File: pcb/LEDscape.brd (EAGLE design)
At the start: 133.3 x 88.9 mm, 30 parts, among them IC1 MAX3041CUE, IC2 MAX3041CUE, IC3 MAX3041CUE, IC4 MAX3041CUE, IC5 MAX3041CUE, IC6 MAX3041CUE, IC7 MAX3041CUE, IC8 MAX3041CUE, X1 44520-0003

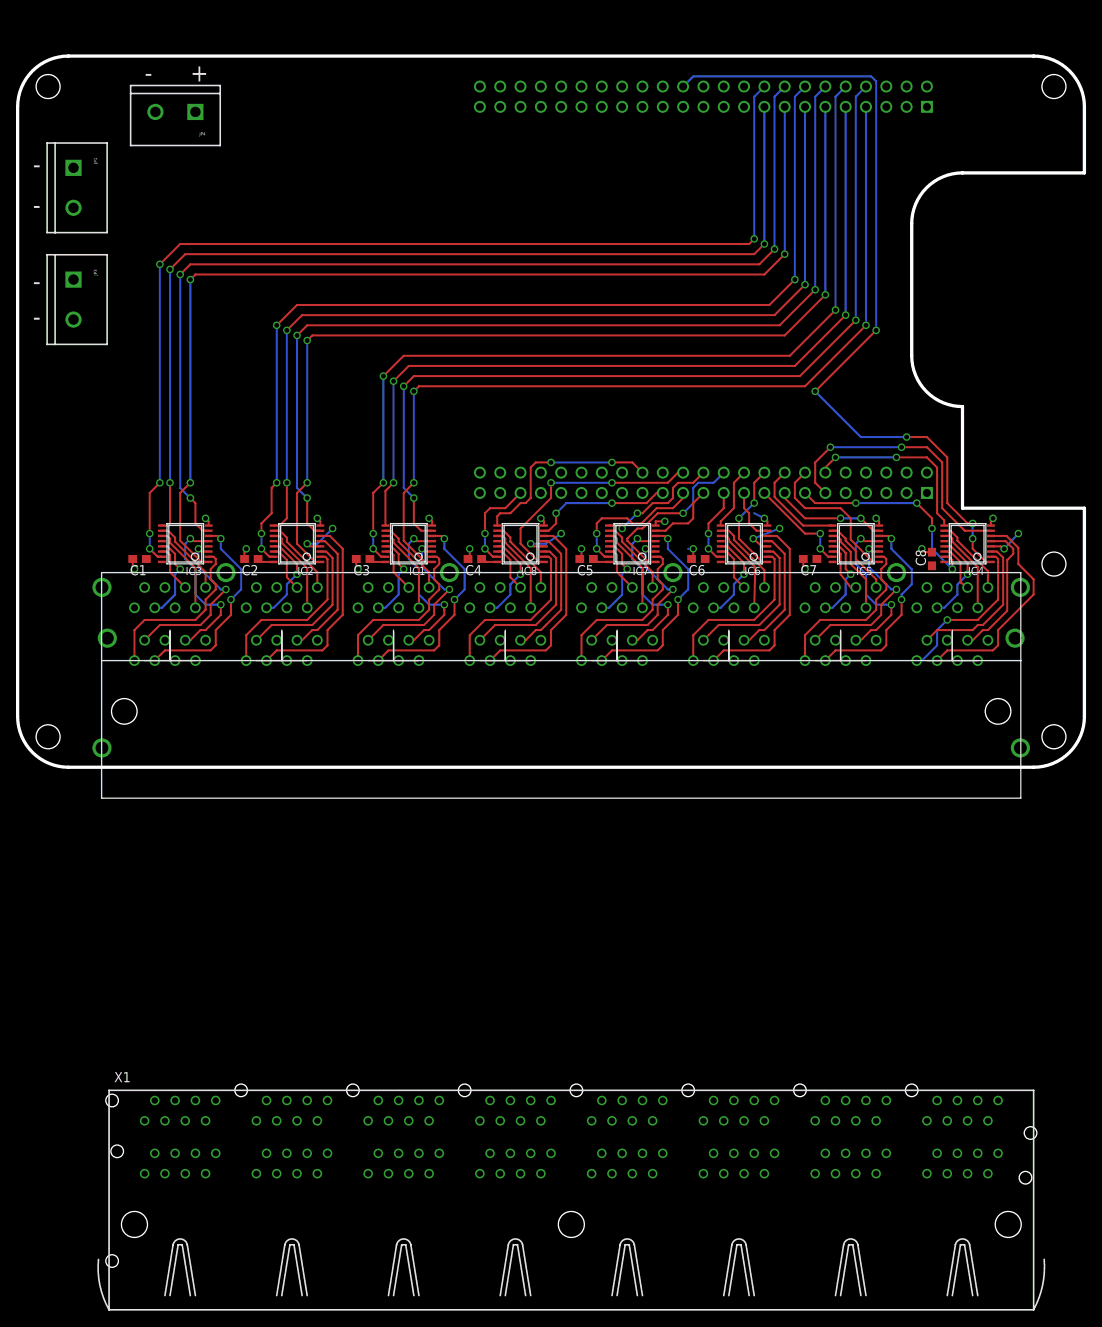
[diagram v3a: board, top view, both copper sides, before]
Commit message: Add some expansion IO (conflicts with HDMI, beware), and fix 8x2 header
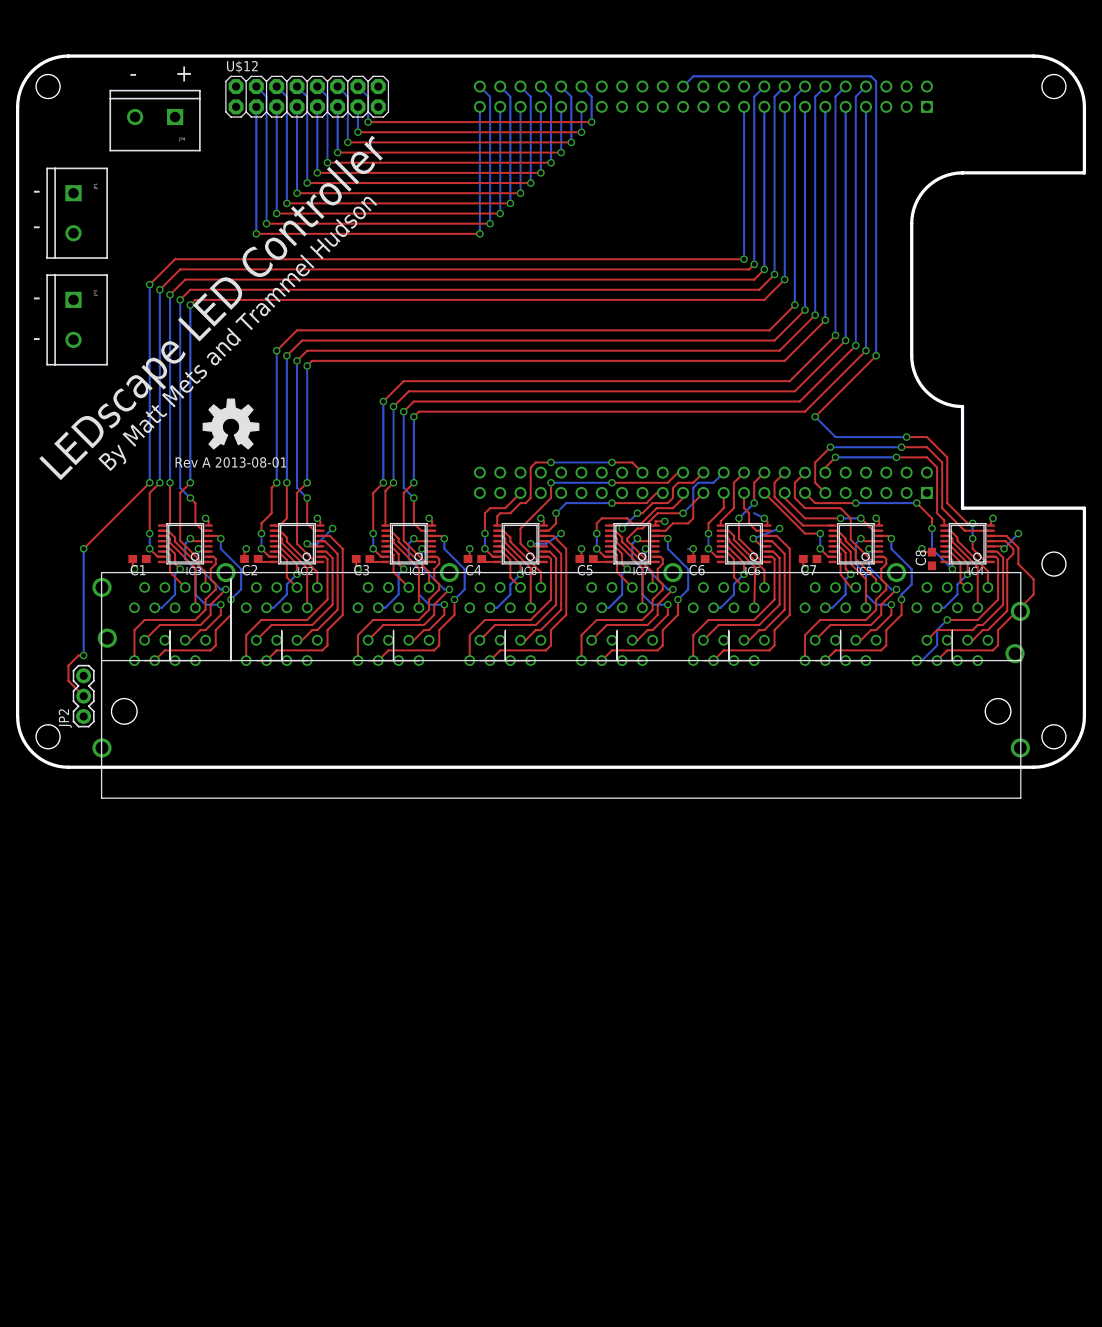
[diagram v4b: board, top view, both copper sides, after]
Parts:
- removed X1: 44520-0003, con-molex:44520-0003
- added JP2: (no value), SparkFun-Connectors:1X03
- added U$11: (no value), blinkiverse:OSHW-LOGO-L
- added U$12: M08X2, SparkFun-Connectors:2X8
- moved JP1 3.18 mm to (6.99, 71.8)
- moved JP4 2.62 mm to (19.7, 81.3)
- moved JP3 2.54 mm to (6.99, 58.4)
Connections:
- new net E0: U$1.45, U$12.3
- new net E1: U$1.46, U$12.4
- new net E10: U$1.35, U$12.13
- new net E11: U$1.36, U$12.14
- new net E2: U$1.43, U$12.5
- new net E3: U$1.44, U$12.6
- new net E4: U$1.41, U$12.7
- new net E5: U$1.42, U$12.8
- new net E6: U$1.39, U$12.9
- new net E7: U$1.40, U$12.10
- new net E8: U$1.37, U$12.11
- new net E9: U$1.38, U$12.12
- new net EXTRA0: JP2.2, U$1.19
- net +5V: now also JP2.1, U$12.1, U$12.2
- net GND: now also JP2.3, U$12.15, U$12.16
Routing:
- net EXTRA0: track 0.00 -> 151.5 mm, vias 0 -> 5
- net E1: track 0.00 -> 63.3 mm, vias 0 -> 2
- net E0: track 0.00 -> 59.7 mm, vias 0 -> 2
- net E3: track 0.00 -> 58.2 mm, vias 0 -> 2
- net E2: track 0.00 -> 54.6 mm, vias 0 -> 2
- net E5: track 0.00 -> 53.1 mm, vias 0 -> 2
- net E4: track 0.00 -> 49.5 mm, vias 0 -> 2
- net E7: track 0.00 -> 48.0 mm, vias 0 -> 2
- net E6: track 0.00 -> 44.4 mm, vias 0 -> 2
- net E9: track 0.00 -> 43.0 mm, vias 0 -> 2
- net E8: track 0.00 -> 39.4 mm, vias 0 -> 2
- net E11: track 0.00 -> 37.9 mm, vias 0 -> 2
- net E10: track 0.00 -> 34.3 mm, vias 0 -> 2
- net S12: track 102.8 -> 104.7 mm
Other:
- board text added: "By Matt Mets and Trammel Hudson"
- board text added: "LEDscape LED Controller"
- board text added: "Rev A 2013-08-01"

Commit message: Small cleanups; take part identifiers off silk, change outline of ethernet to tDocu
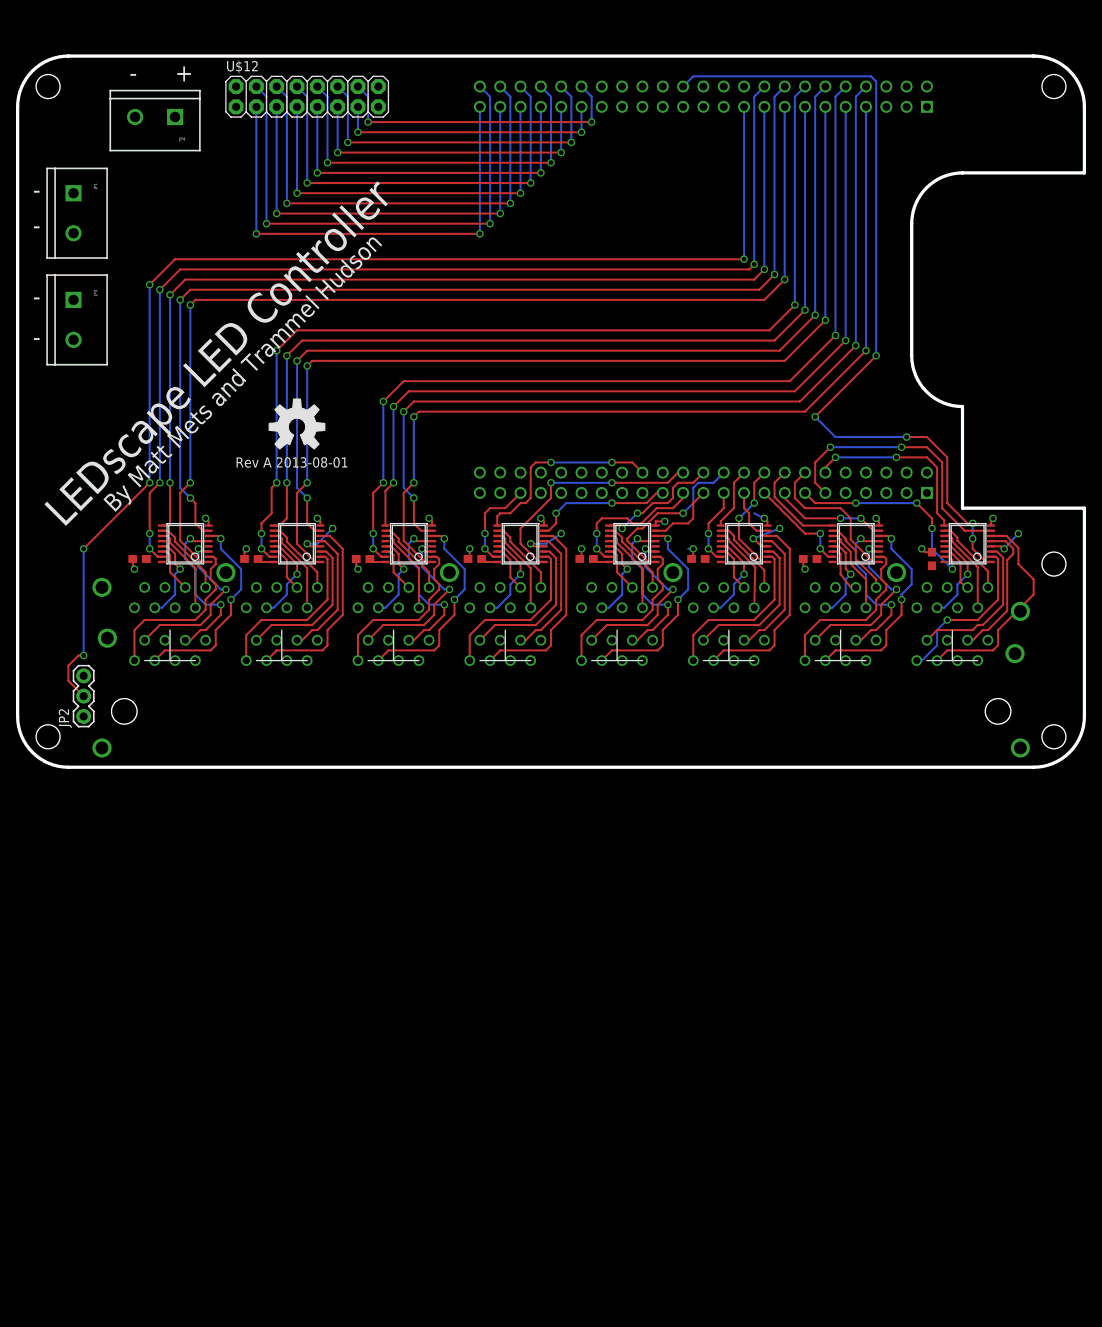
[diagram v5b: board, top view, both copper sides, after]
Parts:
- moved U$11 8.25 mm to (34.9, 42.5)

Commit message: Fix some ERC errors, a sad DRC one, and add an extra GPIO.
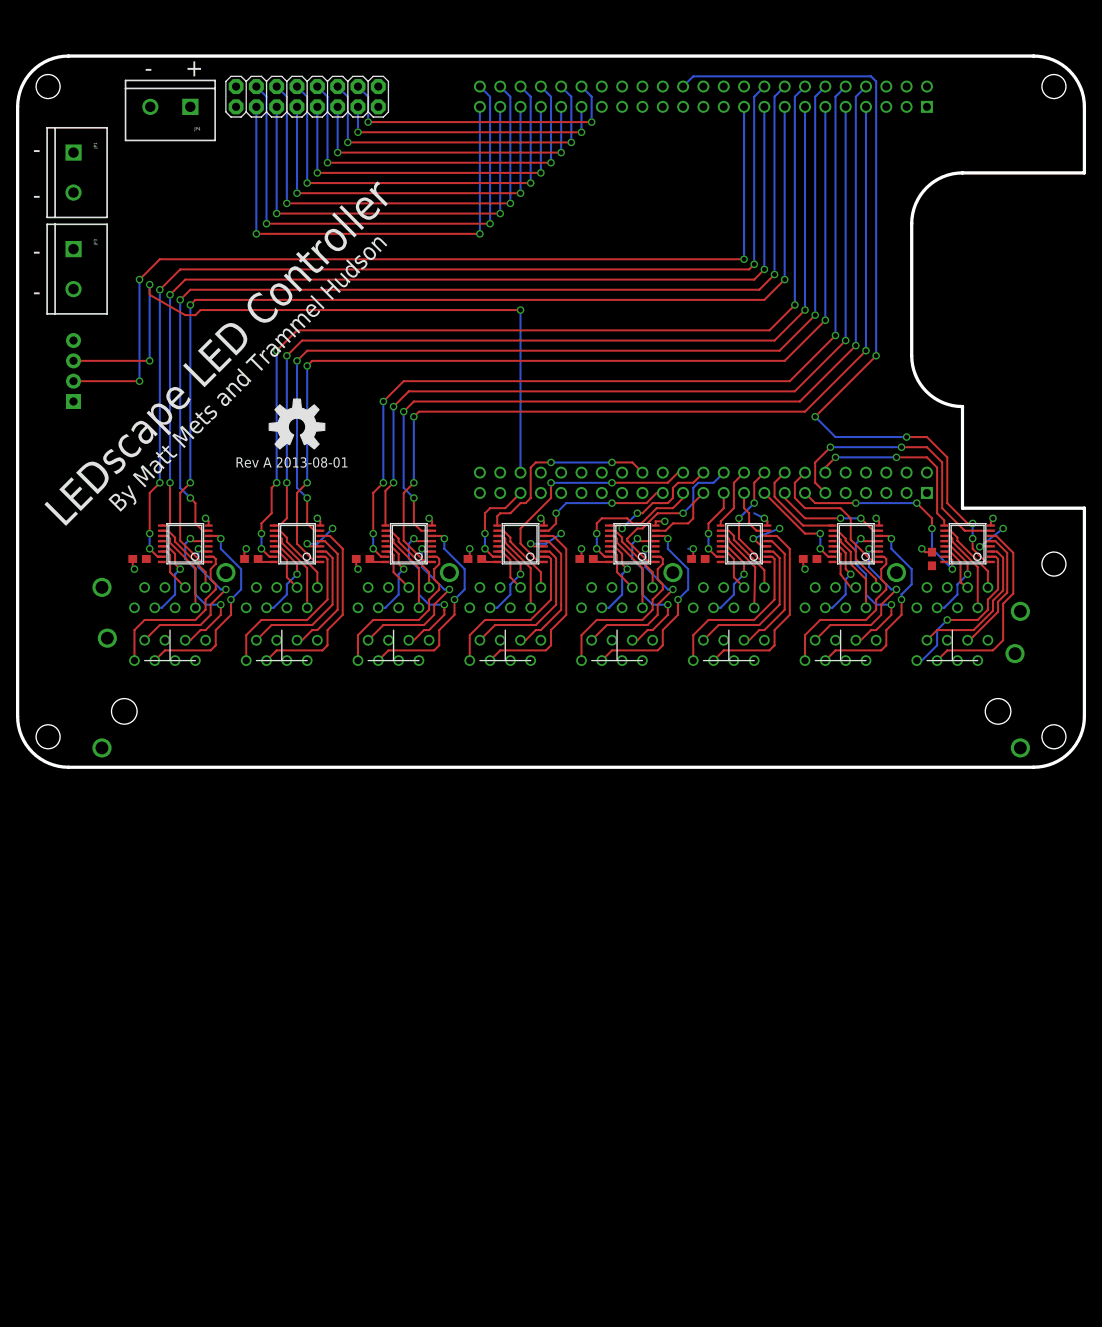
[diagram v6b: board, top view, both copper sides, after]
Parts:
- removed JP2: (no value), SparkFun-Connectors:1X03
- added JP5: (no value), SparkFun-Connectors:1X04_NO_SILK
- moved JP3 6.35 mm to (6.99, 64.8)
- moved JP1 5.08 mm to (6.99, 76.8)
- moved JP4 2.29 mm to (21.6, 82.5)
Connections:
- removed net S32: U$1.88
- new net EXTRA1: JP5.3, U$1.88
- net +5V: now also JP5.1; no longer JP2.1
- net EXTRA0: now also JP5.2; no longer JP2.2
- net GND: now also JP5.4; no longer JP2.3
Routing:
- net EXTRA1: track 0.00 -> 87.9 mm, vias 0 -> 3
- net EXTRA0: track 151.5 -> 116.6 mm, vias 5 -> 3
- net N$29: track 27.3 -> 24.4 mm
- net N$30: track 17.7 -> 15.7 mm
- net +5V: track 31.2 -> 32.0 mm
